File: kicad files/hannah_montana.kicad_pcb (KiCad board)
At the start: 2 copper layers, 220.7 x 67.5 mm, 59 parts, among them J1 Conn_01x04, SW1 SW_Push, U1 ProMicro

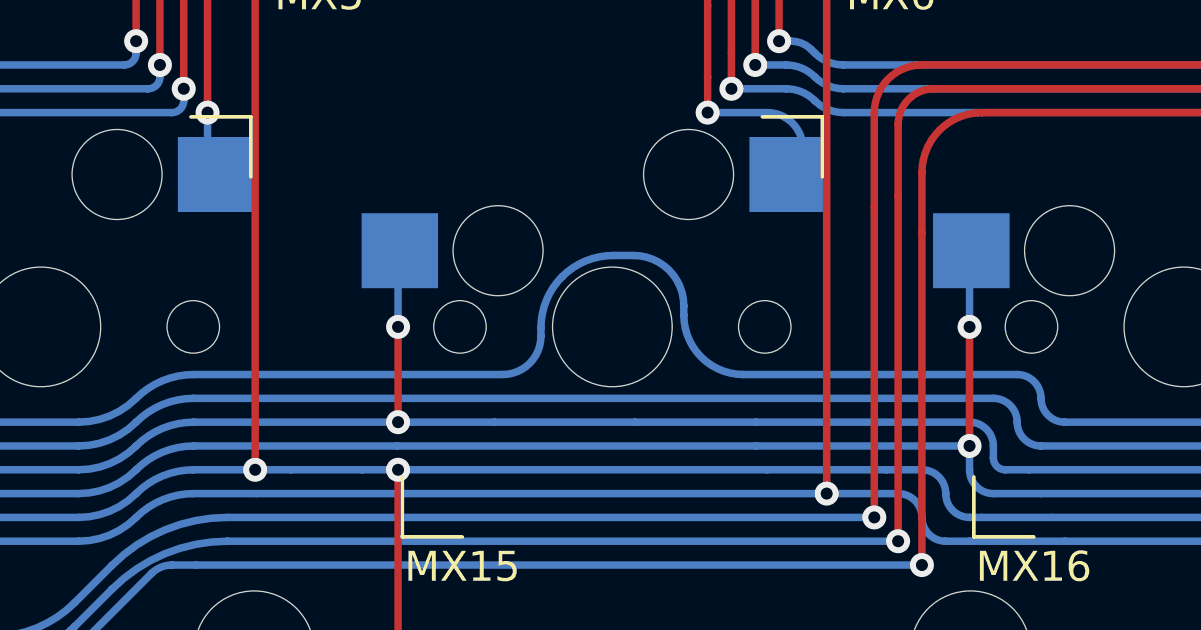
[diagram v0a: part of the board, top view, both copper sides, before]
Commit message: added more art, improved rounding
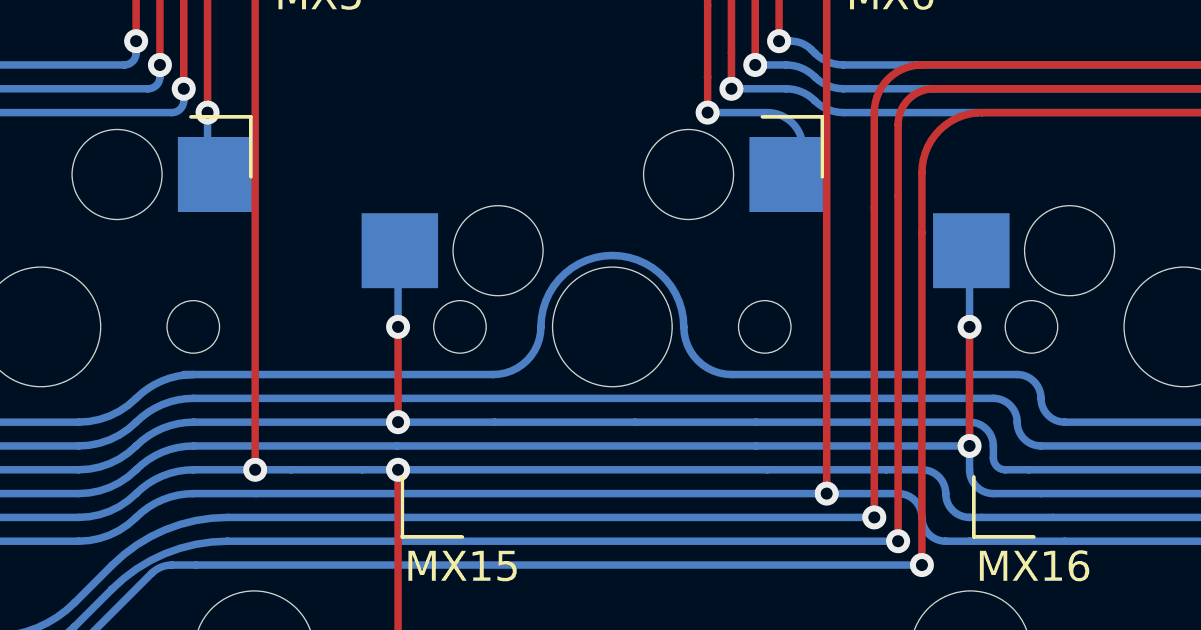
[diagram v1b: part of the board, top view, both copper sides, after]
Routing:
- net col0: track 324.9 -> 292.9 mm
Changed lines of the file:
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@@
       (net 21 "Net-(D18-Pad2)") (pinfunction "A") (pintype "passive"))
   )
+  (gr_arc (start 88.10625 38.89375) (mid 90.4875 36.5125) (end 92.86875 38.89375) (layer "B.Cu") (width 0.25))
+  (gr_arc (start 94.45625 40.48125) (mid 93.333718 40.016282) (end 92.86875 38.89375) (layer "B.Cu") (width 0.25))
+  (gr_line (start 86.51875 40.48125) (end 76.2 40.48125) (layer "B.Cu") (width 0.25))
+  (gr_line (start 94.45625 40.48125) (end 103.98125 40.48125) (layer "B.Cu") (width 0.25))
+  (gr_arc (start 88.10625 38.89375) (mid 87.641282 40.016282) (end 86.51875 40.48125) (layer "B.Cu") (width 0.25))
   (gr_line (start 220.6625 2.38125) (end 220.6625 65.0875) (layer "Edge.Cuts") (width 0.1))
   (gr_arc (start 2.38125 67.46875) (mid 0.697452 66.771298) (end 0 65.0875) (layer "Edge.Cuts") (width 0.1))
@@
   (via (at 130.96875 52.3875) (size 0.8) (drill 0.4) (layers "F.Cu" "B.Cu") (net 41))
   (segment (start 215.112542 23.012457) (end 218.7575 19.3675) (width 0.25) (layer "B.Cu") (net 41))
-  (segment (start 92.86875 38.187227) (end 92.86875 38.496875) (width 0.25) (layer "B.Cu") (net 41))
   (segment (start 161.886894 42.06875) (end 157.543751 42.06875) (width 0.25) (layer "B.Cu") (net 41))
   (segment (start 2.778125 46.0375) (end 2.38125 46.0375) (width 0.25) (layer "B.Cu") (net 41))
@@
   (segment (start 5.159375 45.24375) (end 14.519983 45.24375) (width 0.25) (layer "B.Cu") (net 41))
   (segment (start 52.619983 42.8625) (end 45.24375 42.8625) (width 0.25) (layer "B.Cu") (net 41))
-  (segment (start 88.10625 39.203398) (end 88.10625 38.92472) (width 0.25) (layer "B.Cu") (net 41))
   (segment (start 35.486266 42.8625) (end 45.24375 42.8625) (width 0.25) (layer "B.Cu") (net 41))
-  (segment (start 94.853125 40.48125) (end 103.98125 40.48125) (width 0.25) (layer "B.Cu") (net 41))
-  (segment (start 86.828398 40.48125) (end 76.528782 40.48125) (width 0.25) (layer "B.Cu") (net 41))
   (segment (start 130.96875 52.3875) (end 130.96875 55.5625) (width 0.25) (layer "B.Cu") (net 41))
   (segment (start 130.96875 42.06875) (end 120.253125 42.06875) (width 0.25) (layer "B.Cu") (net 41))
@@
   (segment (start 17.065625 44.45) (end 16.271875 44.45) (width 0.25) (layer "B.Cu") (net 41))
   (segment (start 130.96875 42.06875) (end 138.150606 42.06875) (width 0.25) (layer "B.Cu") (net 41))
-  (segment (start 91.194023 36.5125) (end 90.51847 36.5125) (width 0.25) (layer "B.Cu") (net 41))
   (segment (start 3.455632 45.756866) (end 3.688116 45.524383) (width 0.25) (layer "B.Cu") (net 41))
   (segment (start 45.24375 38.89375) (end 45.24375 35.71875) (width 0.25) (layer "B.Cu") (net 41))
@@
   (arc (start 104.775 41.275) (mid 105.007483 41.836266) (end 105.56875 42.06875) (width 0.25) (layer "B.Cu") (net 41))
   (arc (start 54.536266 42.06875) (mid 54.017723 42.171894) (end 53.578125 42.465625) (width 0.25) (layer "B.Cu") (net 41))
-  (arc (start 90.51847 36.5125) (mid 89.595353 36.696119) (end 88.812773 37.219023) (width 0.25) (layer "B.Cu") (net 41))
   (arc (start 25.003125 44.053125) (mid 24.563525 44.346855) (end 24.044983 44.45) (width 0.25) (layer "B.Cu") (net 41))
-  (arc (start 88.812773 37.219023) (mid 88.289869 38.001603) (end 88.10625 38.92472) (width 0.25) (layer "B.Cu") (net 41))
   (arc (start 15.478124 44.846874) (mid 15.038525 45.140605) (end 14.519983 45.24375) (width 0.25) (layer "B.Cu") (net 41))
   (arc (start 76.528782 40.48125) (mid 75.491697 40.687538) (end 74.6125 41.275) (width 0.25) (layer "B.Cu") (net 41))
   (arc (start 213.51875 31.337501) (mid 212.932963 32.751713) (end 211.518751 33.3375) (width 0.25) (layer "B.Cu") (net 41))
-  (arc (start 92.86875 38.187227) (mid 92.378233 37.003016) (end 91.194023 36.5125) (width 0.25) (layer "B.Cu") (net 41))
   (arc (start 4.365625 45.24375) (mid 3.99896 45.316684) (end 3.688116 45.524383) (width 0.25) (layer "B.Cu") (net 41))
   (arc (start 34.528125 43.259375) (mid 34.088525 43.553105) (end 33.569983 43.65625) (width 0.25) (layer "B.Cu") (net 41))
-  (arc (start 92.86875 38.496875) (mid 93.449959 39.90004) (end 94.853125 40.48125) (width 0.25) (layer "B.Cu") (net 41))
   (arc (start 176.2125 43.259375) (mid 176.561225 44.101274) (end 177.403125 44.45) (width 0.25) (layer "B.Cu") (net 41))
   (arc (start 16.271875 44.45) (mid 15.90521 44.522934) (end 15.594366 44.730633) (width 0.25) (layer "B.Cu") (net 41))
-  (arc (start 88.10625 39.203398) (mid 87.731975 40.106975) (end 86.828398 40.48125) (width 0.25) (layer "B.Cu") (net 41))
   (arc (start 74.6125 41.275) (mid 73.733302 41.862461) (end 72.696217 42.06875) (width 0.25) (layer "B.Cu") (net 41))
   (arc (start 215.112542 23.012457) (mid 213.932963 24.777822) (end 213.51875 26.860213) (width 0.25) (layer "B.Cu") (net 41))

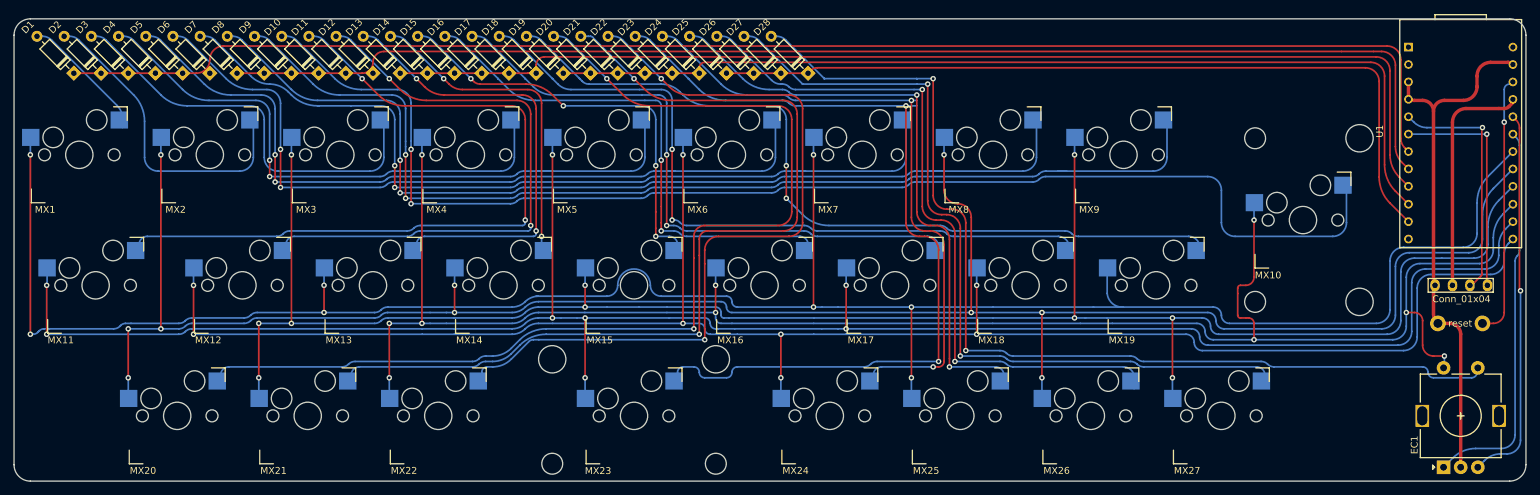
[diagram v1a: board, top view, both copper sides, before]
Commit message: fixed problems with routing
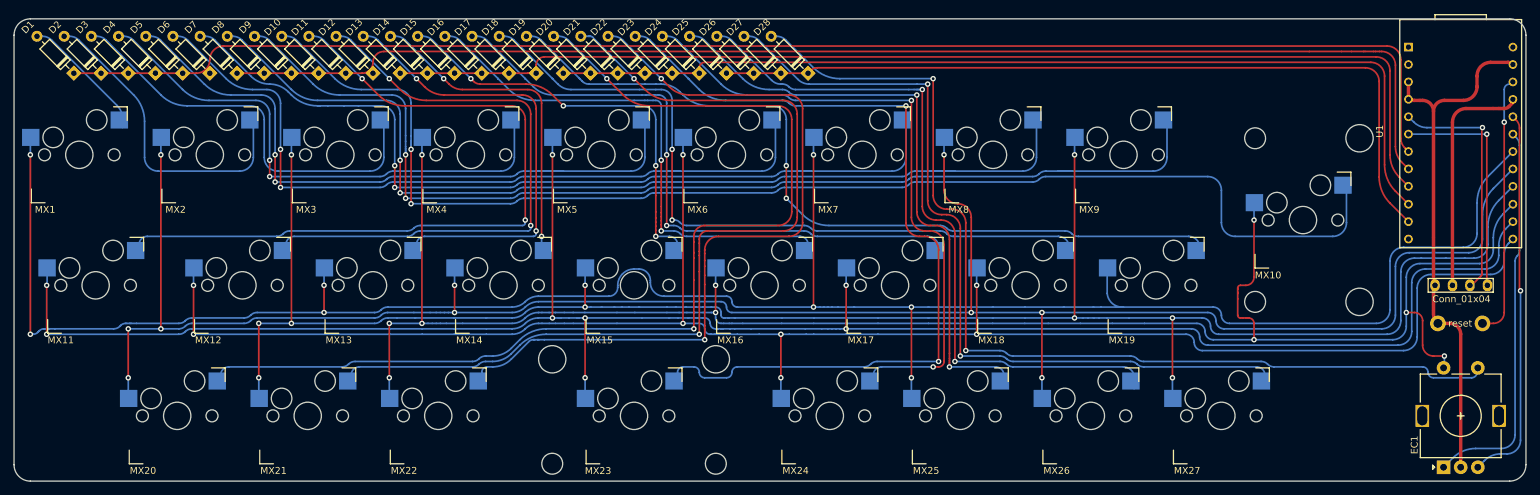
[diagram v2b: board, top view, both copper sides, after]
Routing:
- net col0: track 292.9 -> 324.9 mm
- net Net-(D8-Pad2): track 144.4 -> 145.9 mm
- net Net-(D5-Pad2): track 97.6 -> 99.2 mm
- net Net-(D23-Pad2): track 126.2 -> 124.6 mm
- net Net-(D9-Pad2): track 159.7 -> 160.5 mm
- net Net-(D7-Pad2): track 126.3 -> 127.0 mm
- net Net-(D6-Pad2): track 112.9 -> 113.7 mm
- net Net-(D24-Pad2): track 94.1 -> 93.3 mm

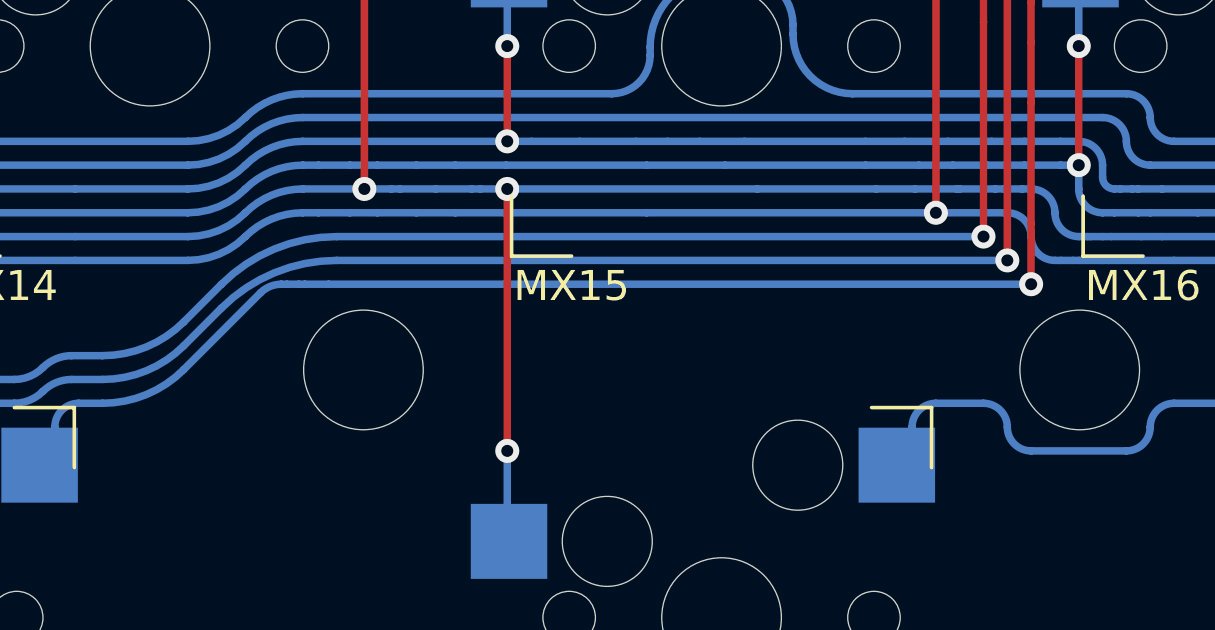
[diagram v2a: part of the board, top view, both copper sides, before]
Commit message: fixed more problems with routing
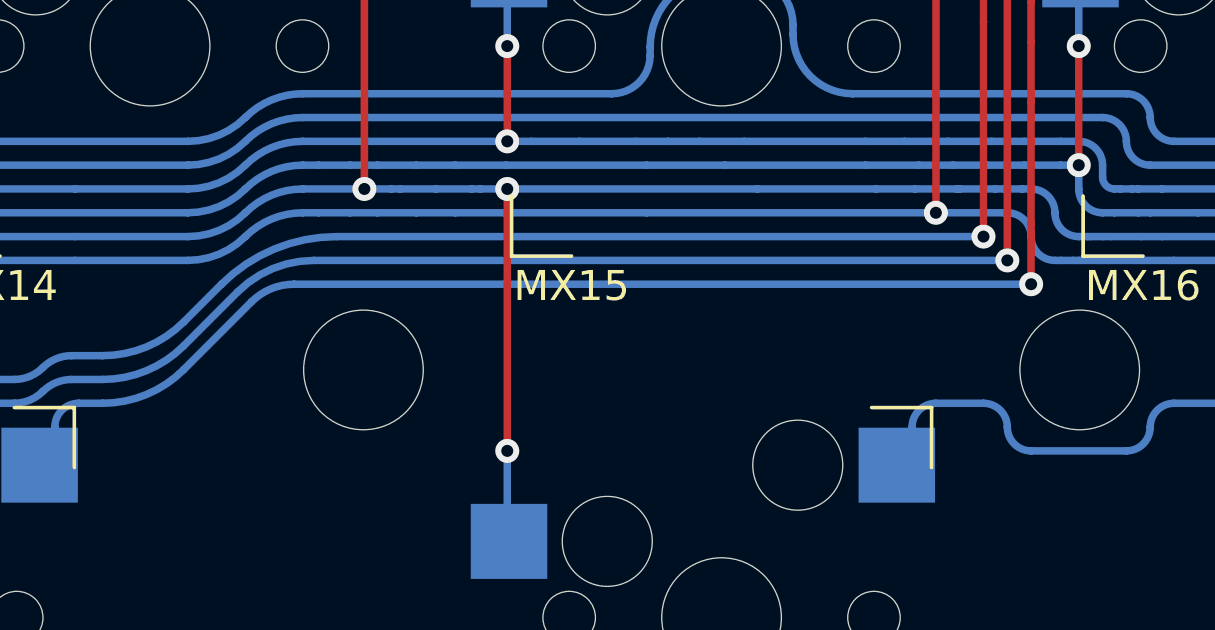
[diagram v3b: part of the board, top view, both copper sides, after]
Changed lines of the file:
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@@
   (segment (start 83.799902 2.549346) (end 83.884653 2.549346) (width 0.25) (layer "B.Cu") (net 25))
   (segment (start 83.460898 2.549346) (end 82.718096 2.549346) (width 0.25) (layer "B.Cu") (net 25))
-  (segment (start 72.560031 48.883717) (end 73.812457 47.631292) (width 0.25) (layer "B.Cu") (net 25))
+  (segment (start 72.560031 48.883717) (end 74.349533 47.094217) (width 0.25) (layer "B.Cu") (net 25))
   (segment (start 90.4875 8.729844) (end 90.4875 8.73125) (width 0.25) (layer "B.Cu") (net 25))
   (segment (start 84.054155 2.549346) (end 83.884653 2.549346) (width 0.25) (layer "B.Cu") (net 25))
@@
   (segment (start 50.403125 50.8) (end 66.907483 50.8) (width 0.25) (layer "B.Cu") (net 25))
   (segment (start 49.2125 51.990625) (end 49.2125 53.18125) (width 0.25) (layer "B.Cu") (net 25))
-  (segment (start 77.660213 46.0375) (end 100.0125 46.0375) (width 0.25) (layer "B.Cu") (net 25))
+  (segment (start 76.900673 46.0375) (end 100.0125 46.0375) (width 0.25) (layer "B.Cu") (net 25))
   (segment (start 83.799902 2.549346) (end 83.460898 2.549346) (width 0.25) (layer "B.Cu") (net 25))
   (segment (start 90.486505 8.727443) (end 84.428264 2.669202) (width 0.25) (layer "B.Cu") (net 25))
@@
   (arc (start 49.2125 51.990625) (mid 49.561225 51.148725) (end 50.403125 50.8) (width 0.25) (layer "B.Cu") (net 25))
   (arc (start 69.85 50.00625) (mid 71.316658 49.714513) (end 72.560031 48.883717) (width 0.25) (layer "B.Cu") (net 25))
-  (arc (start 77.660213 46.0375) (mid 75.577822 46.451713) (end 73.812457 47.631292) (width 0.25) (layer "B.Cu") (net 25))
+  (arc (start 76.900673 46.0375) (mid 75.520006 46.312132) (end 74.349533 47.094217) (width 0.25) (layer "B.Cu") (net 25))
   (arc (start 68.823766 50.00625) (mid 68.305223 50.109394) (end 67.865625 50.403125) (width 0.25) (layer "B.Cu") (net 25))
   (arc (start 66.907483 50.8) (mid 67.426025 50.696855) (end 67.865625 50.403125) (width 0.25) (layer "B.Cu") (net 25))
@@
   (arc (start 115.09375 29.750001) (mid 114.507963 31.164213) (end 113.093751 31.75) (width 0.25) (layer "F.Cu") (net 26))
   (segment (start 87.482002 2.549346) (end 86.686846 2.549346) (width 0.25) (layer "B.Cu") (net 26))
-  (segment (start 77.390625 46.83125) (end 76.596875 46.83125) (width 0.25) (layer "B.Cu") (net 26))
+  (segment (start 76.234675 46.83125) (end 100.80625 46.83125) (width 0.25) (layer "B.Cu") (net 26))
+  (segment (start 74.820461 47.417037) (end 72.560031 49.677467) (width 0.25) (layer "B.Cu") (net 26))
   (segment (start 94.45625 8.729844) (end 94.45625 8.73125) (width 0.25) (layer "B.Cu") (net 26))
-  (segment (start 75.125616 47.111883) (end 72.560031 49.677467) (width 0.25) (layer "B.Cu") (net 26))
-  (segment (start 76.001562 46.83125) (end 75.803125 46.83125) (width 0.25) (layer "B.Cu") (net 26))
-  (segment (start 100.80625 46.83125) (end 77.390625 46.83125) (width 0.25) (layer "B.Cu") (net 26))
   (segment (start 68.2625 51.59375) (end 68.2625 52.3875) (width 0.25) (layer "B.Cu") (net 26))
   (segment (start 69.85 50.8) (end 69.05625 50.8) (width 0.25) (layer "B.Cu") (net 26))
-  (segment (start 76.398437 46.83125) (end 76.596875 46.83125) (width 0.25) (layer "B.Cu") (net 26))
   (segment (start 94.455255 8.727443) (end 88.839418 3.111606) (width 0.25) (layer "B.Cu") (net 26))
-  (segment (start 76.398437 46.83125) (end 76.001562 46.83125) (width 0.25) (layer "B.Cu") (net 26))
   (arc (start 68.2625 51.59375) (mid 68.494983 51.032483) (end 69.05625 50.8) (width 0.25) (layer "B.Cu") (net 26))
   (arc (start 87.482002 2.549346) (mid 88.21663 2.695472) (end 88.839418 3.111606) (width 0.25) (layer "B.Cu") (net 26))
+  (arc (start 76.234675 46.83125) (mid 75.469308 46.983491) (end 74.820461 47.417037) (width 0.25) (layer "B.Cu") (net 26))
   (arc (start 94.455255 8.727443) (mid 94.455991 8.728544) (end 94.45625 8.729844) (width 0.25) (layer "B.Cu") (net 26))
-  (arc (start 75.125616 47.111883) (mid 75.43646 46.904184) (end 75.803125 46.83125) (width 0.25) (layer "B.Cu") (net 26))
   (arc (start 69.85 50.8) (mid 71.316658 50.508263) (end 72.560031 49.677467) (width 0.25) (layer "B.Cu") (net 26))
   (segment (start 132.174998 31.75) (end 132.937501 31.75) (width 0.25) (layer "F.Cu") (net 27))
